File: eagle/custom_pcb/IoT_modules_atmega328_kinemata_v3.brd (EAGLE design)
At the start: 51 x 35 mm, 54 parts, among them IC2 4093DT, Q3 MOSFET-P, T1 2N2222, U2 ATMEGA328P, U3 FT232RL-BASICSSOP, U4 MCP73831, Y2 8MHz

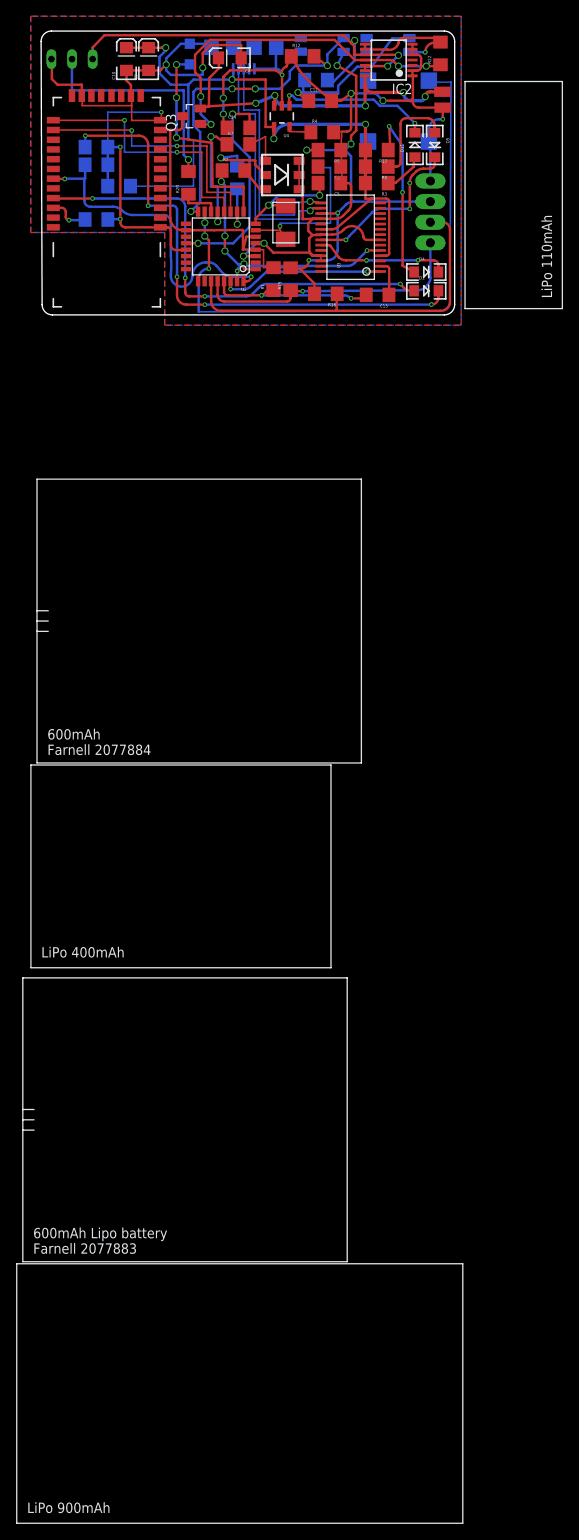
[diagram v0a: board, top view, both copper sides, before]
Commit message: custom pcb wiring passing drc
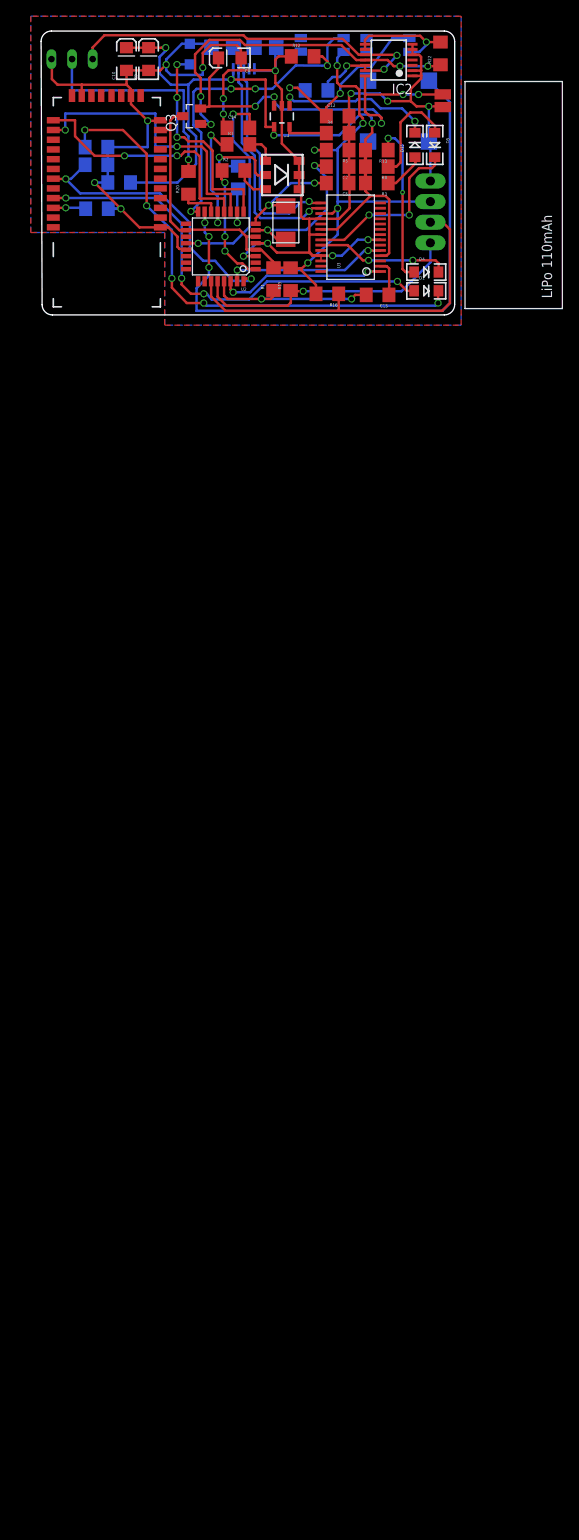
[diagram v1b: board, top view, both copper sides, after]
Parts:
- removed U$6: LIPO_BATTERY300MAH, MlabPaja_v3:LIPO_BATTERY_300MAH_FARNELL_2077884
- removed U$7: LIPO_BATTERY400MAH, MlabPaja_v3:LIPO_BATTERY_400MAH
- removed U$8: LIPO_BATTERY600MAH, MlabPaja_v3:LIPO_BATTERY_600MAH_FARNELL_2077883
- removed U$9: LIPO_BATTERY900MAH, MlabPaja_v3:LIPO_BATTERY_900MAH
- moved C12 2.88 mm to (36.6, 24.5)
- moved R4 1.91 mm to (36.6, 22.4)
- moved R10 1.34 mm to (6.90, 13.1)
- moved R21 1.27 mm to (34.0, 27.7)
- moved C2 1.02 mm to (36.6, 18.3)
- moved C5 1.02 mm to (36.6, 16.3)
- moved R5 1.02 mm to (36.6, 20.3)
- moved C7 0.44 mm to (9.63, 16.3)
- moved BAT+2 0.32 mm to (49.5, 27.2)
- moved R16 0.19 mm to (35.3, 2.60)
- moved R6 0.13 mm to (24.3, 16.9)
- moved BAT-1 0.07 mm to (49.5, 25.6)
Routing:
- net GND: track 224.5 -> 208.7 mm, vias 13 -> 15
- net VCC: track 43.5 -> 49.5 mm
- net BT_TX: track 31.9 -> 35.6 mm
- net IS_CON: track 38.8 -> 35.8 mm
- net 3.3V: track 94.4 -> 91.5 mm
- net D+USB: track 29.1 -> 26.6 mm
- net D-USB: track 29.9 -> 27.5 mm
- net PWR2: track 21.6 -> 23.8 mm, vias 1 -> 2
- net PROG: track 3.21 -> 5.31 mm
- net N$7: track 22.3 -> 20.4 mm
- net N$1: track 5.15 -> 3.68 mm
- net N$23: track 54.4 -> 52.9 mm
- net PWR1: track 15.2 -> 13.9 mm
- net BUZZER: track 74.4 -> 73.2 mm
- net N$17: track 65.3 -> 64.2 mm
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
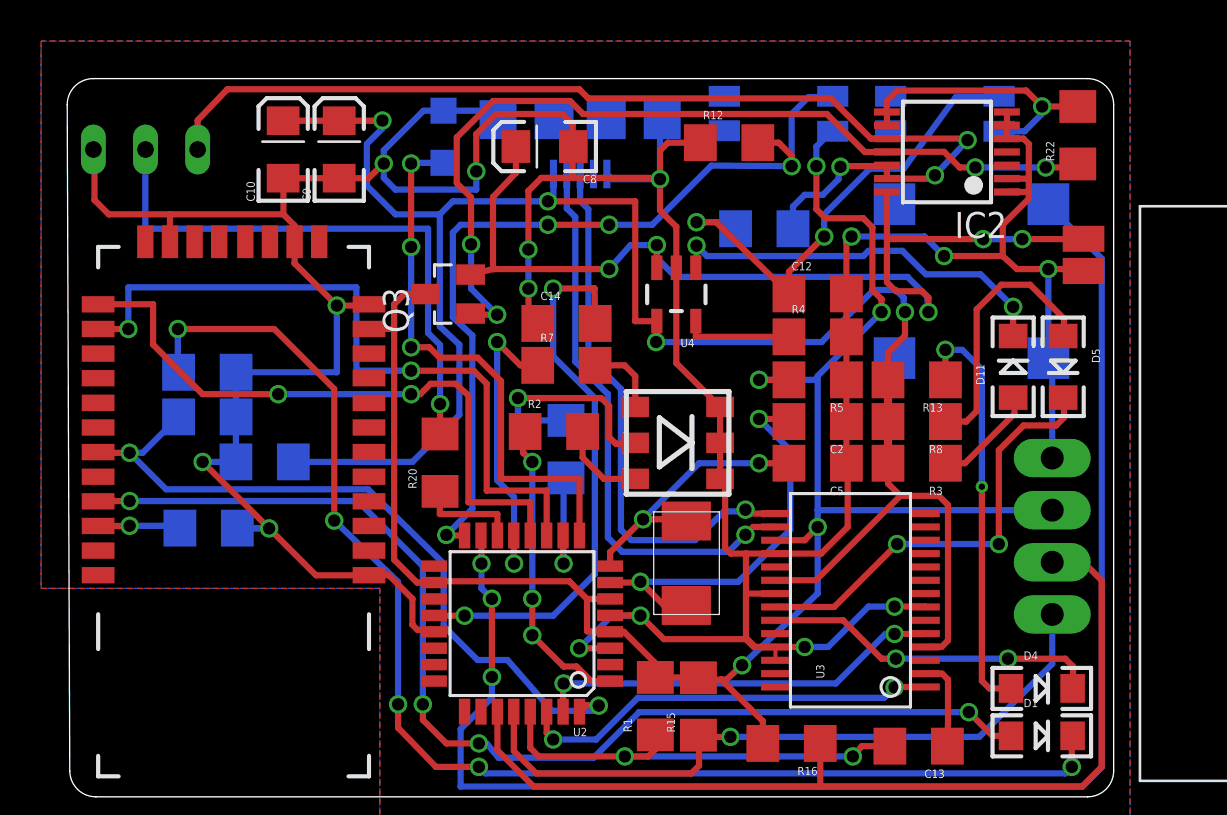
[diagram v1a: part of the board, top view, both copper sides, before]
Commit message: tweaked positioning and minor issues on custom PCB
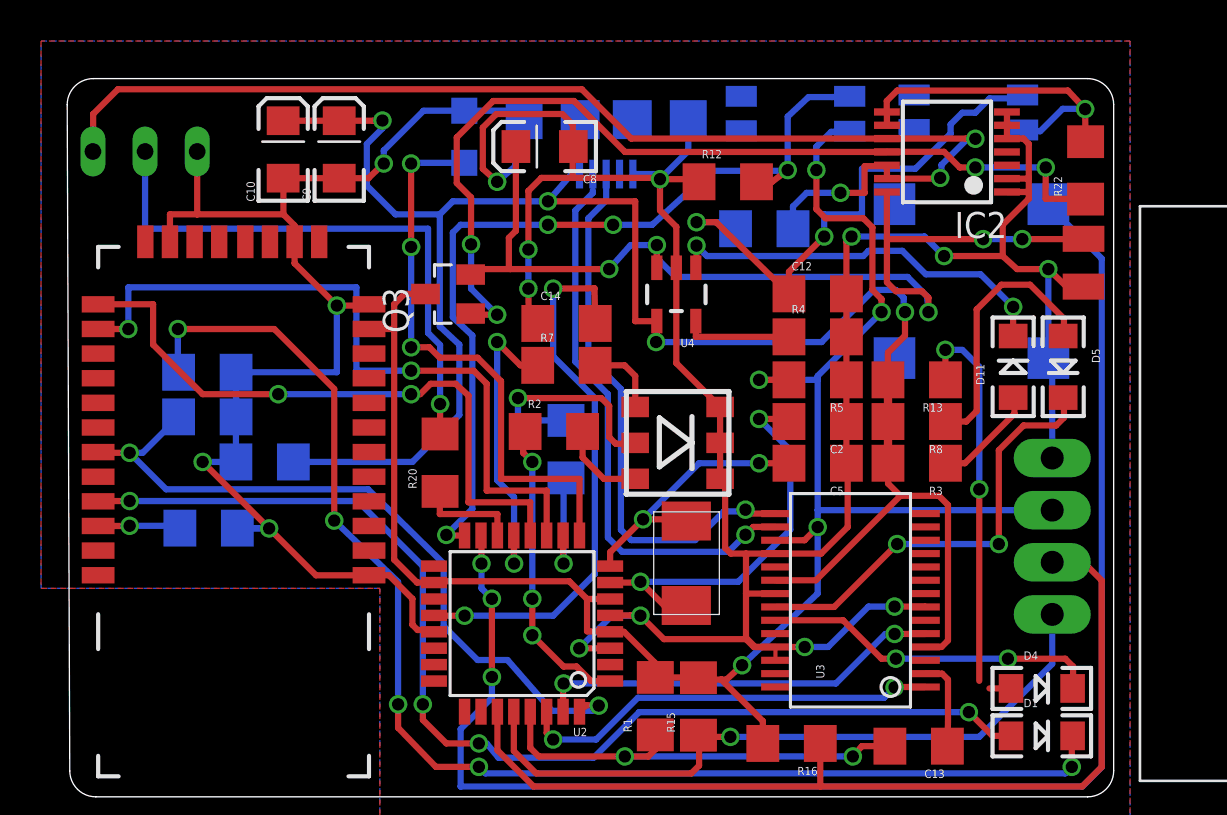
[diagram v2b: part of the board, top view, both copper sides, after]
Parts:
- moved T1 2.44 mm to (3.80, 32.7), turned to 0 degrees
- moved R12 1.91 mm to (32.2, 30.0)
- moved R22 1.76 mm to (49.6, 30.5)
- moved JP6 1.27 mm to (26.3, 33.0)
- moved U$4 1.27 mm to (15.9, 32.4)
- moved S1 1.14 mm to (43.9, 33.6)
- moved U$5 1.02 mm to (19.4, 32.2)
- moved S2 0.83 mm to (35.5, 33.5)
- moved BAT-1 0.76 mm to (49.5, 24.9)
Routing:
- net N$23: track 52.9 -> 59.8 mm
- net GND: track 208.7 -> 202.5 mm
- net PWR1: track 13.9 -> 16.6 mm
- net PWR2: track 23.8 -> 26.2 mm
- net N$27: track 43.2 -> 45.0 mm
- net VIBE: track 27.0 -> 28.0 mm
- net 3.3V: track 91.5 -> 92.2 mm
- net D-USB: track 27.5 -> 26.9 mm
- net N$7: track 20.4 -> 19.8 mm
- net 5V: track 92.7 -> 93.2 mm

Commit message: custom pcb pre print
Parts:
- moved U$5 7.40 mm to (15.1, 26.1), turned to 0 degrees
- moved D4 4.59 mm to (44.7, 8.89), turned to 270 degrees
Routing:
- net VIBE: track 28.0 -> 20.8 mm, vias 3 -> 1
- net N$7: track 19.8 -> 14.1 mm
- net DTR: track 4.46 -> 8.70 mm
- net TXLED: track 16.5 -> 13.0 mm
- net GND: track 202.5 -> 206.0 mm, vias 15 -> 16
- net N$24: track 27.8 -> 29.8 mm
- net SCL: track 34.3 -> 35.1 mm
- net 5V: track 93.2 -> 93.9 mm
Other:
- outline, holes or cut-outs redrawn
